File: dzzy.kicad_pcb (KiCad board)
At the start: 2 copper layers, 114.5 x 100.5 mm, 96 parts, among them J1 JTAG/SWD, P1 PC, U1 USBLC6-2SC6, U2 XC6206P332MR, U3 M95256-WMN6P, U4 GD32VF103CBT6

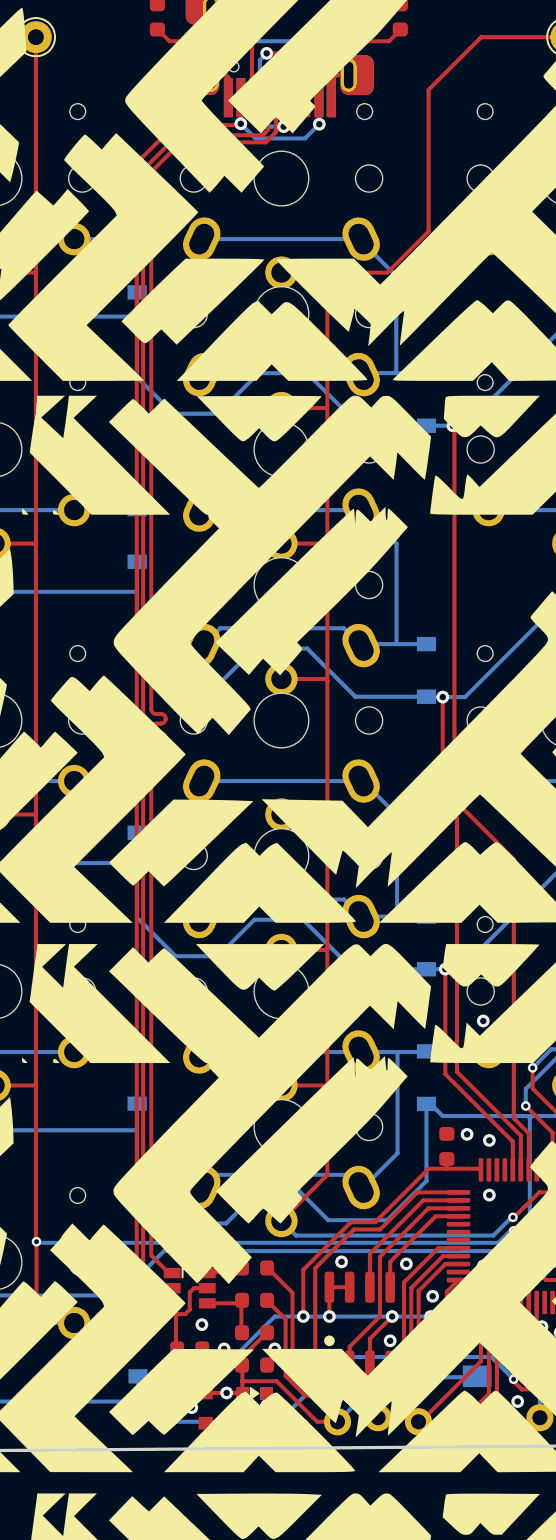
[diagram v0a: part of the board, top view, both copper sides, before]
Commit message: Update ESD diode placement and silkscreen
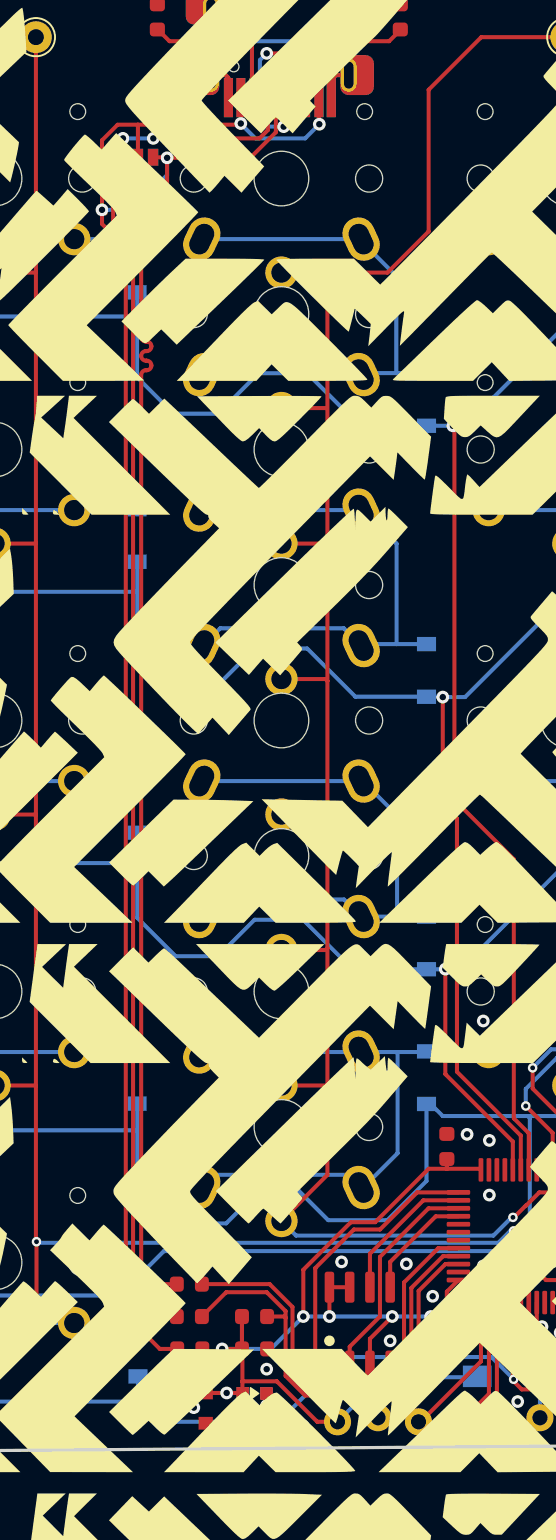
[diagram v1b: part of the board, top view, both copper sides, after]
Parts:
- U1: value USBLC6-2SC6 -> USBLC6-4SC6; footprint prettylib:SOT-23-6 -> prettylib:SOT-23-6_flipable
- U3: value M95256-WMN6P -> M95512-WMN6P
- moved U1 69.9 mm to (88.7, 32.8), turned to 90 degrees
- moved R7 4.21 mm to (91.9, 104.4)
- moved R6 4.21 mm to (91.9, 102.4)
- moved C13 1.02 mm to (96.0, 106.4)
- moved R2 1.02 mm to (96.0, 104.4), turned to 180 degrees
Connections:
- R2 pad 1: USB_D_ESD+ -> /USB_D_R+
- R6 pad 1: USB_D_ESD- -> USB_D-
- R7 pad 1: USB_D_ESD+ -> USB_D+
- U1 pad 1: USB_D- -> unconnected-(U1-Pad1)
- U1 pad 3: USB_D+ -> unconnected-(U1-Pad3)
- U1 pad 4: USB_D_ESD+ -> USB_D-
- U1 pad 6: USB_D_ESD- -> USB_D+
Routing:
- net USB_D+: track 91.9 -> 99.7 mm, vias 1 -> 3
- net /USB_D_R+: track 23.8 -> 30.2 mm
- net USB_VBUS: track 102.7 -> 108.8 mm, vias 2 -> 3
- net USB_D_ESD+: track 3.98 -> 0.00 mm
- net /USB_D_R-: track 25.3 -> 28.5 mm
- net USB_D-: track 90.1 -> 93.2 mm, vias 1 -> 2
- net VDD: track 92.4 -> 94.9 mm
- net USB_D_ESD-: track 1.72 -> 0.00 mm
- net VSS: vias 35 -> 33
